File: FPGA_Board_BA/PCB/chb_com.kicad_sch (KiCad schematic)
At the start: 9 parts, among them J10 Box_Header_26pin, J11 Box_Header_26pin, J12 Box_Header_2x05_THT, J13 Box_Header_2x05_THT, J14 Box_Header_2x05_THT, J15 Box_Header_2x05_THT, J16 Box_Header_26pin, J17 Box_Header_26pin, J18 Plug_Terminal_2x12pin

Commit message: exported stuff
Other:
- note added: "24 pin Wannenstecker von Mouser könnte hier passen"

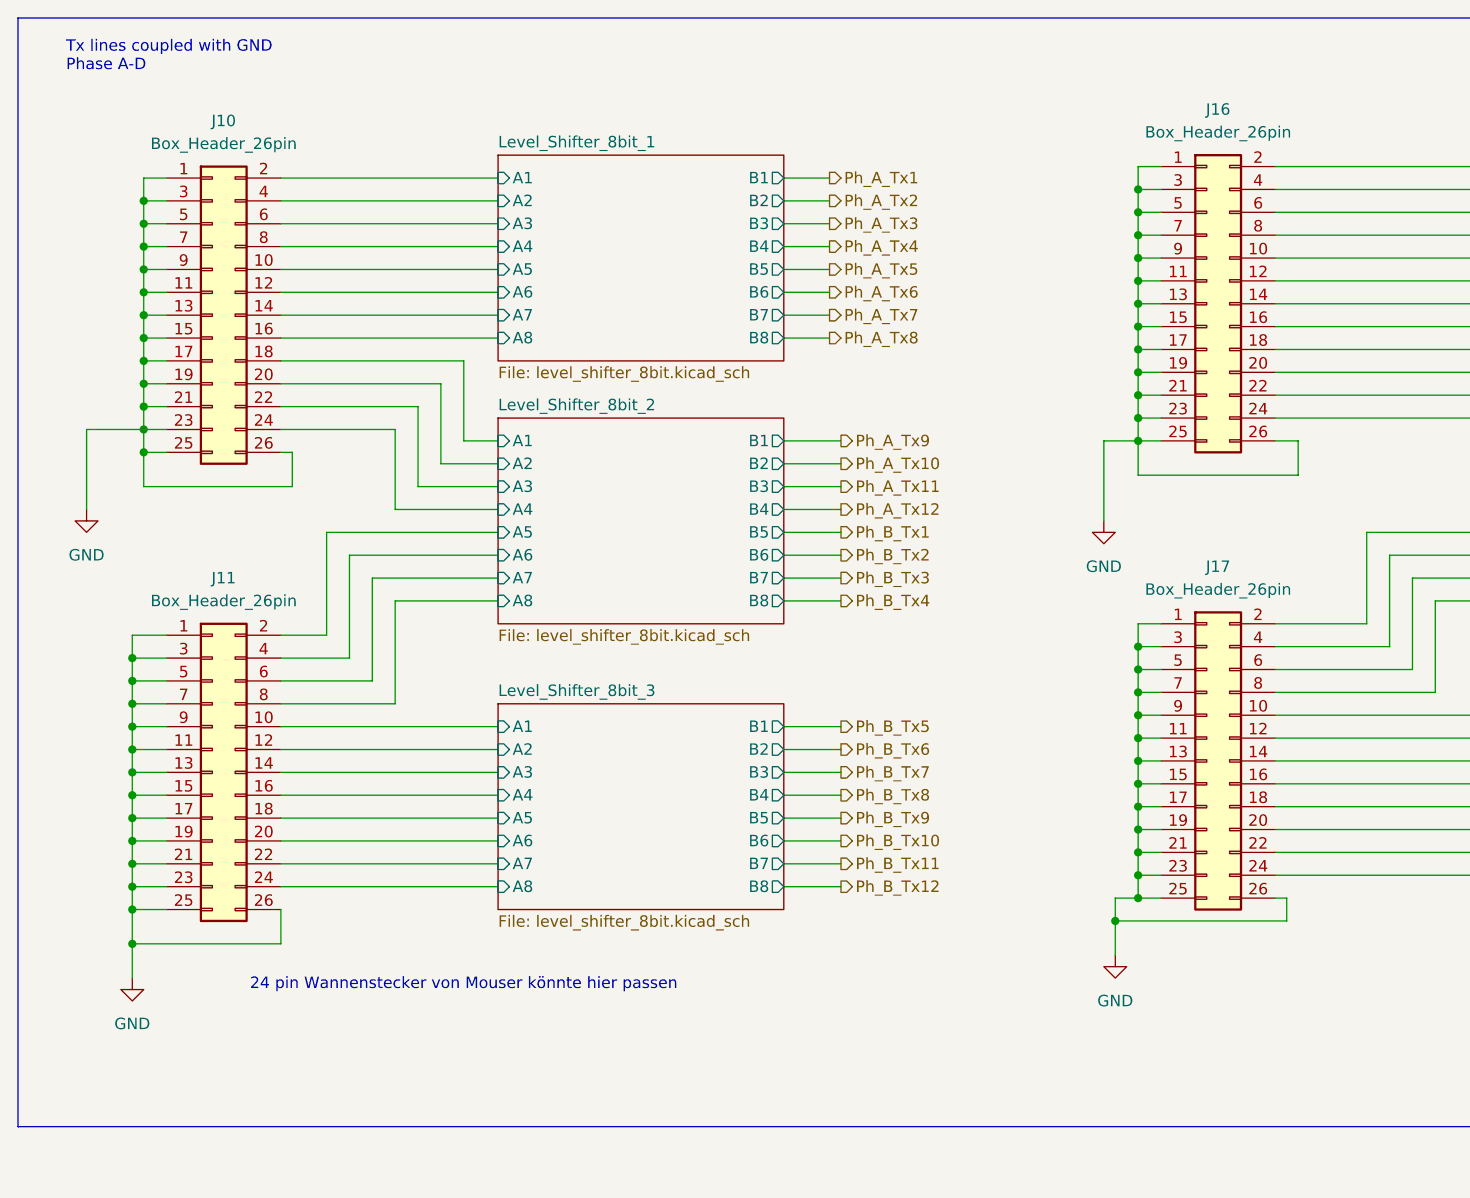
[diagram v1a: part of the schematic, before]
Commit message: added Wannenstecker 24pin + BOM
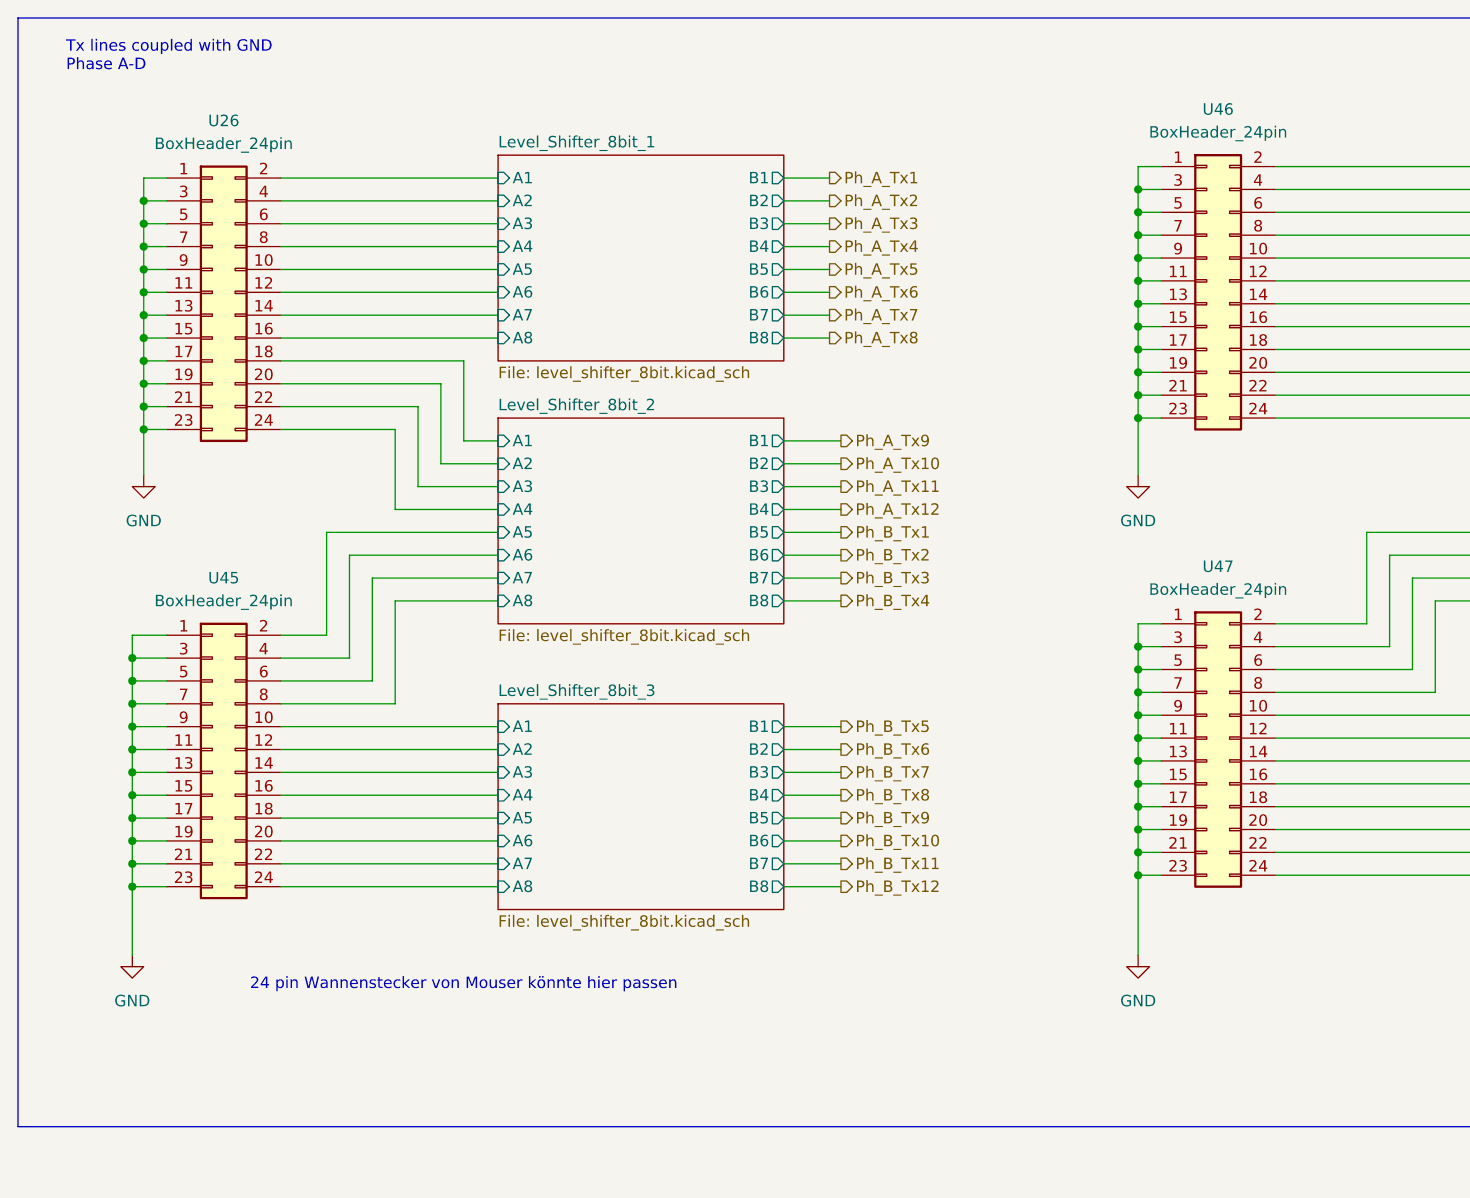
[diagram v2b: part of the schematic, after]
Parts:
- removed J10, J11, J16, J17: Box_Header_26pin, Connector_IDC:IDC-Header_2x13_P2.54mm_Vertical, symbol MYLIB_Misc:Box_Header_26pin
- added U26, U45, U46, U47: BoxHeader_24pin, Connector_IDC:IDC-Header_2x12_P2.54mm_Vertical_SMD, symbol MYLIB_Misc:Box_Header_24pin
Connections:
- net GND: now also U26.1, U26.11, U26.13, U26.15, U26.17, U26.19, U26.21, U26.23, U26.3, U26.5, U26.7, U26.9, U45.1, U45.11, U45.13, U45.15, U45.17, U45.19, U45.21, U45.23, U45.3, U45.5, U45.7, U45.9, U46.1, U46.11, U46.13, U46.15, U46.17, U46.19, U46.21, U46.23, U46.3, U46.5, U46.7, U46.9, U47.1, U47.11, U47.13, U47.15, U47.17, U47.19, U47.21, U47.23, U47.3, U47.5, U47.7, U47.9
- net Level_Shifter_8bit_1/A1: now also U26.2
- net Level_Shifter_8bit_1/A2: now also U26.4
- net Level_Shifter_8bit_1/A3: now also U26.6
- net Level_Shifter_8bit_1/A4: now also U26.8
- net Level_Shifter_8bit_1/A5: now also U26.10
- net Level_Shifter_8bit_1/A6: now also U26.12
- net Level_Shifter_8bit_1/A7: now also U26.14
- net Level_Shifter_8bit_1/A8: now also U26.16
- net Level_Shifter_8bit_2/A1: now also U26.18
- net Level_Shifter_8bit_2/A2: now also U26.20
- net Level_Shifter_8bit_2/A3: now also U26.22
- net Level_Shifter_8bit_2/A4: now also U26.24
- net Level_Shifter_8bit_2/A5: now also U45.2
- net Level_Shifter_8bit_2/A6: now also U45.4
- net Level_Shifter_8bit_2/A7: now also U45.6
- net Level_Shifter_8bit_2/A8: now also U45.8
- net Level_Shifter_8bit_3/A1: now also U45.10
- net Level_Shifter_8bit_3/A2: now also U45.12
- net Level_Shifter_8bit_3/A3: now also U45.14
- net Level_Shifter_8bit_3/A4: now also U45.16
- net Level_Shifter_8bit_3/A5: now also U45.18
- net Level_Shifter_8bit_3/A6: now also U45.20
- net Level_Shifter_8bit_3/A7: now also U45.22
- net Level_Shifter_8bit_3/A8: now also U45.24
- net Level_Shifter_8bit_4/A1: now also U46.2
- net Level_Shifter_8bit_4/A2: now also U46.4
- net Level_Shifter_8bit_4/A3: now also U46.6
- net Level_Shifter_8bit_4/A4: now also U46.8
- net Level_Shifter_8bit_4/A5: now also U46.10
- net Level_Shifter_8bit_4/A6: now also U46.12
- net Level_Shifter_8bit_4/A7: now also U46.14
- net Level_Shifter_8bit_4/A8: now also U46.16
- net Level_Shifter_8bit_5/A1: now also U46.18
- net Level_Shifter_8bit_5/A2: now also U46.20
- net Level_Shifter_8bit_5/A3: now also U46.22
- net Level_Shifter_8bit_5/A4: now also U46.24
- net Level_Shifter_8bit_5/A5: now also U47.2
- net Level_Shifter_8bit_5/A6: now also U47.4
- net Level_Shifter_8bit_5/A7: now also U47.6
- net Level_Shifter_8bit_5/A8: now also U47.8
- net Level_Shifter_8bit_6/A1: now also U47.10
- net Level_Shifter_8bit_6/A2: now also U47.12
- net Level_Shifter_8bit_6/A3: now also U47.14
- net Level_Shifter_8bit_6/A4: now also U47.16
- net Level_Shifter_8bit_6/A5: now also U47.18
- net Level_Shifter_8bit_6/A6: now also U47.20
- net Level_Shifter_8bit_6/A7: now also U47.22
- net Level_Shifter_8bit_6/A8: now also U47.24

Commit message: right side almost finished
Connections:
- net Level_Shifter_8bit_1/A8 is gone; now on net Level_Shifter_8bit_1/A1: U26.16
- net Level_Shifter_8bit_2/A4 is gone; now on net Level_Shifter_8bit_2/A5: U26.24
- net Level_Shifter_8bit_4/A8 is gone; now on net Level_Shifter_8bit_4/A1: U46.16
- net Level_Shifter_8bit_5/A4 is gone; now on net Level_Shifter_8bit_5/A5: U46.24
- net Level_Shifter_8bit_1/A1: no longer U26.2
- net Level_Shifter_8bit_1/A2: now also U26.14; no longer U26.4
- net Level_Shifter_8bit_1/A3: now also U26.12; no longer U26.6
- net Level_Shifter_8bit_1/A4: now also U26.10; no longer U26.8
- net Level_Shifter_8bit_1/A5: now also U26.8; no longer U26.10
- net Level_Shifter_8bit_1/A6: now also U26.6; no longer U26.12
- net Level_Shifter_8bit_1/A7: now also U26.4; no longer U26.14
- net Level_Shifter_8bit_2/A1: now also U45.8; no longer U26.18
- net Level_Shifter_8bit_2/A2: now also U45.6; no longer U26.20
- net Level_Shifter_8bit_2/A3: now also U45.4; no longer U26.22
- net Level_Shifter_8bit_2/A5: no longer U45.2
- net Level_Shifter_8bit_2/A6: now also U26.22; no longer U45.4
- net Level_Shifter_8bit_2/A7: now also U26.20; no longer U45.6
- net Level_Shifter_8bit_2/A8: now also U26.18; no longer U45.8
- net Level_Shifter_8bit_3/A1: now also U45.24; no longer U45.10
- net Level_Shifter_8bit_3/A2: now also U45.22; no longer U45.12
- net Level_Shifter_8bit_3/A3: now also U45.20; no longer U45.14
- net Level_Shifter_8bit_3/A4: now also U45.18; no longer U45.16
- net Level_Shifter_8bit_3/A5: now also U45.16; no longer U45.18
- net Level_Shifter_8bit_3/A6: now also U45.14; no longer U45.20
- net Level_Shifter_8bit_3/A7: now also U45.12; no longer U45.22
- net Level_Shifter_8bit_3/A8: now also U45.10; no longer U45.24
- net Level_Shifter_8bit_4/A1: no longer U46.2
- net Level_Shifter_8bit_4/A2: now also U46.14; no longer U46.4
- net Level_Shifter_8bit_4/A3: now also U46.12; no longer U46.6
- net Level_Shifter_8bit_4/A4: now also U46.10; no longer U46.8
- net Level_Shifter_8bit_4/A5: now also U46.8; no longer U46.10
- net Level_Shifter_8bit_4/A6: now also U46.6; no longer U46.12
- net Level_Shifter_8bit_4/A7: now also U46.4; no longer U46.14
- net Level_Shifter_8bit_5/A1: now also U47.8; no longer U46.18
- net Level_Shifter_8bit_5/A2: now also U47.6; no longer U46.20
- net Level_Shifter_8bit_5/A3: now also U47.4; no longer U46.22
- net Level_Shifter_8bit_5/A5: no longer U47.2
- net Level_Shifter_8bit_5/A6: now also U46.22; no longer U47.4
- net Level_Shifter_8bit_5/A7: now also U46.20; no longer U47.6
- net Level_Shifter_8bit_5/A8: now also U46.18; no longer U47.8
- net Level_Shifter_8bit_6/A1: now also U47.24; no longer U47.10
- net Level_Shifter_8bit_6/A2: now also U47.22; no longer U47.12
- net Level_Shifter_8bit_6/A3: now also U47.20; no longer U47.14
- net Level_Shifter_8bit_6/A4: now also U47.18; no longer U47.16
- net Level_Shifter_8bit_6/A5: now also U47.16; no longer U47.18
- net Level_Shifter_8bit_6/A6: now also U47.14; no longer U47.20
- net Level_Shifter_8bit_6/A7: now also U47.12; no longer U47.22
- net Level_Shifter_8bit_6/A8: now also U47.10; no longer U47.24
- net Ph_A_Tx1: no longer J12.3 (Pin_3)
- net Ph_B_Tx1: no longer J13.3 (Pin_3)
- net Ph_C_Tx1: no longer J14.3 (Pin_3)
- net Ph_D_Tx1: no longer J15.3 (Pin_3)
- new net Ph_A_Tx1_5V: J12.3 (Pin_3), U26.2
- new net Ph_B_Tx1_5V: J13.3 (Pin_3), U45.2
- new net Ph_C_Tx1_5V: J14.3 (Pin_3), U46.2
- new net Ph_D_Tx1_5V: J15.3 (Pin_3), U47.2
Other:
- moved on the sheet: J12, J13, J14, J15, U26, U45, U46, U47

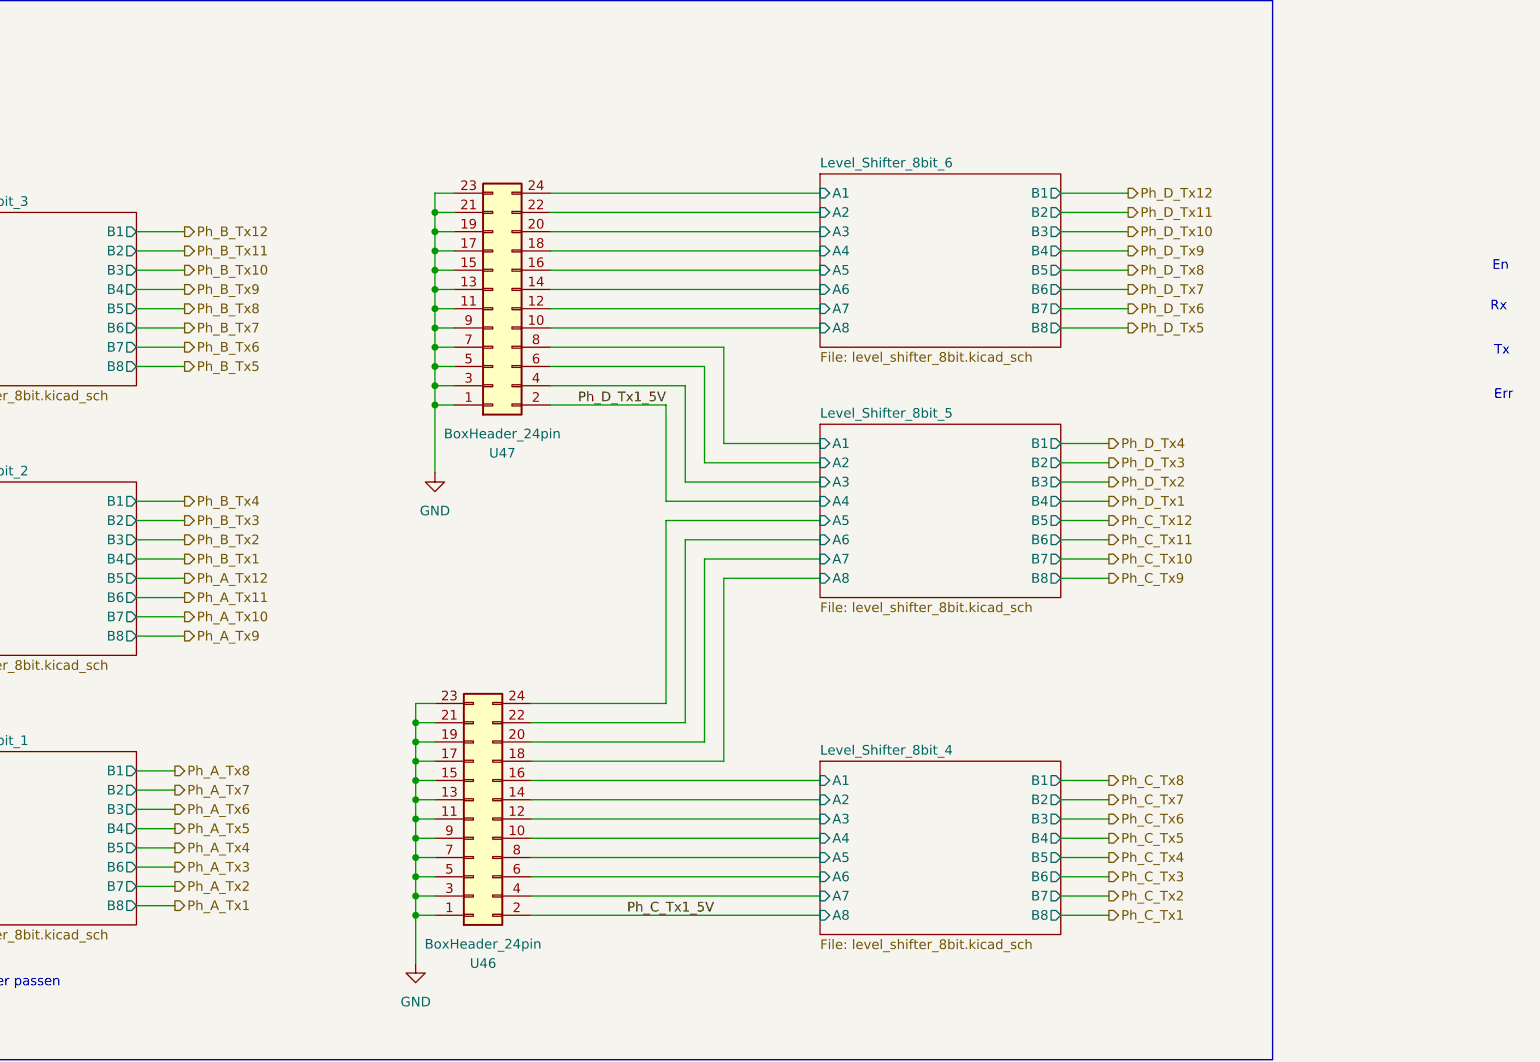
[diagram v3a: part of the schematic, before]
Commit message: added bus into schematic
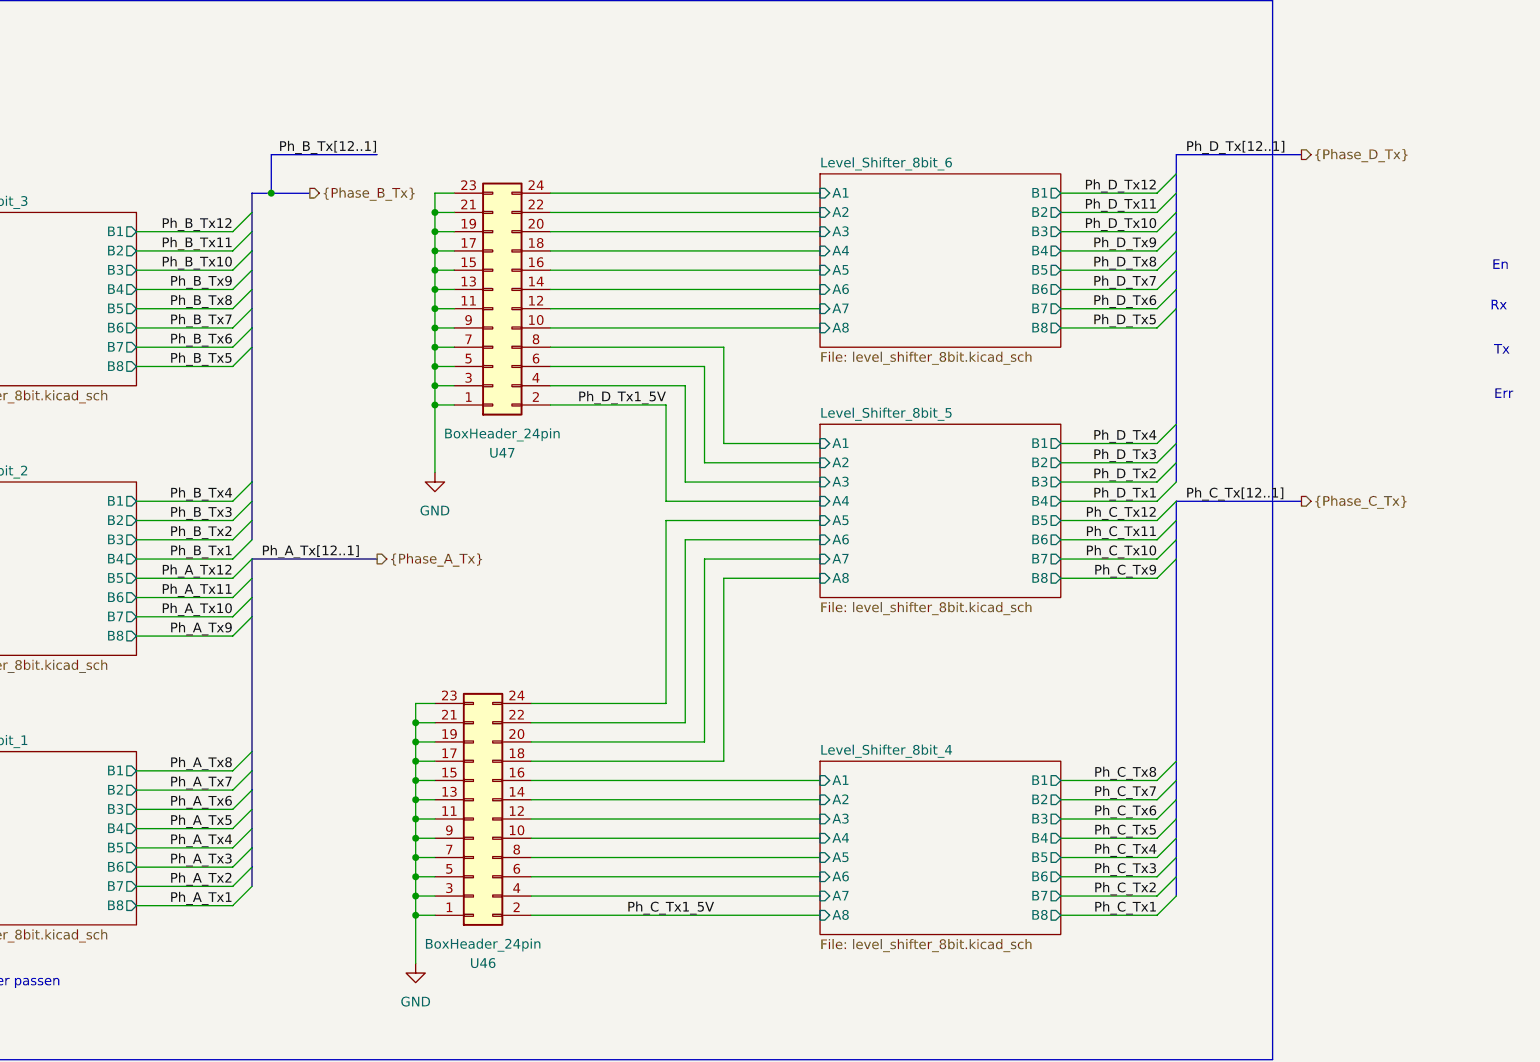
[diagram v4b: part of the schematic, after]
